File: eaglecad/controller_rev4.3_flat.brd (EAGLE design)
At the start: 40 x 29.5 mm, 79 parts, among them U100 STM32L452XX_QFPN48, U101 TCAN330, U200 TPS63070, U300 STSPIN230, U301 TSV991ILT, U302 AS5047P, U400 STSPIN250, U401 TSV991ILT, X101 ABM10-16MHz

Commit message: board flattening
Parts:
- added TP1, TP10, TP11, TP12, TP13, TP14, TP15, TP16, TP17, TP18, TP19, TP2, TP20, TP21, TP22, TP23, TP24, TP25, TP26, TP27, TP28, TP29, TP3, TP30, TP31, TP4, TP5, TP6, TP7, TP8, TP9: TEST-POINT-LARGE, oresat-misc:1X01
- moved C204 79.1 mm to (-11.7, 58.7), flipped to the bottom, turned to 180 degrees
- moved R203 79.1 mm to (-13.6, 58.7), flipped to the bottom, turned to 0 degrees
- moved R205 78.9 mm to (-10.2, 58.5), flipped to the bottom, turned to 270 degrees
- moved C207 78.4 mm to (-8.71, 58.1), flipped to the bottom, turned to 90 degrees
- moved R202 78.4 mm to (-15.5, 58.1), flipped to the bottom, turned to 180 degrees
- moved C202 78.1 mm to (-17.8, 57.9), flipped to the bottom, turned to 90 degrees
- moved R201 77.1 mm to (-15.2, 57.1), flipped to the bottom, turned to 0 degrees
- moved U200 76.6 mm to (-12.5, 56.7), flipped to the bottom, turned to 270 degrees
- moved R204 76.6 mm to (-10.2, 56.6), flipped to the bottom, turned to 270 degrees
- moved C401 75.0 mm to (51.1, 76.3), flipped to the bottom, turned to 90 degrees
- moved C402 75.0 mm to (49.6, 76.3), flipped to the bottom, turned to 90 degrees
- moved C403 75.0 mm to (48.1, 76.3), flipped to the bottom, turned to 90 degrees
- moved C203 74.7 mm to (-15.9, 55.1), flipped to the bottom, turned to 270 degrees
- moved C205 74.5 mm to (-8.96, 54.9), flipped to the bottom, turned to 270 degrees
- moved C206 74.2 mm to (-7.21, 54.6), flipped to the bottom, turned to 270 degrees
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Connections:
- net 3.3V: now also TP29.1, TP30.1, TP31.1
- net ADDR_0: now also TP14.1
- net ADDR_1: now also TP15.1
- net BLDC_CURR_FDB: now also TP2.1
- net BLDC_EN: now also TP11.1
- net BLDC_FAULT: now also TP10.1
- net BLDC_INUH: now also TP23.1
- net BLDC_INUL: now also TP7.1
- net BLDC_INVH: now also TP24.1
- net BLDC_INVL: now also TP8.1
- net BLDC_INWH: now also TP25.1
- net BLDC_INWL: now also TP9.1
- net BLDC_STBY: now also TP22.1
- net CAN_RX: now also TP27.1
- net CAN_SILENT: now also TP28.1
- net CAN_TX: now also TP26.1
- net DEBUG_1: now also TP13.1
- net DEBUG_2: now also TP6.1
- net I2C_SCL: now also TP20.1
- net I2C_SDA: now also TP21.1
- net MAG_CURR_FDB: now also TP1.1
- net MAG_DIR: now also TP16.1
- net MAG_EN: now also TP19.1
- net MAG_FAULT: now also TP18.1
- net MAG_PWM: now also TP12.1
- net MAG_STBY: now also TP17.1
- net SPI1_CS: now also TP3.1
- net SPI1_MISO: now also TP5.1
- net SPI1_SCK: now also TP4.1
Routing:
- net GND: track 59.1 -> 0.00 mm, vias 179 -> 0
- net 3.3V: track 29.8 -> 0.00 mm, vias 18 -> 0
- net I2C_SCL: track 26.9 -> 0.00 mm, vias 2 -> 0
- net BLDC_CURR_FDB: track 25.8 -> 0.00 mm, vias 2 -> 0
- net I2C_SDA: track 25.1 -> 0.00 mm, vias 2 -> 0
- net BOOT: track 19.7 -> 0.00 mm, vias 2 -> 0
- net MAG_CURR_FDB: track 17.8 -> 0.00 mm, vias 2 -> 0
- net SWCLK: track 17.6 -> 0.00 mm, vias 2 -> 0
- net SWDIO: track 17.3 -> 0.00 mm, vias 2 -> 0
- net SENSE_BLDC: track 16.6 -> 0.00 mm, vias 3 -> 0
- net OUT1: track 15.8 -> 0.00 mm, vias 3 -> 0
- net BLDC_STBY: track 15.7 -> 0.00 mm, vias 2 -> 0
- net SPI1_CS: track 14.8 -> 0.00 mm, vias 1 -> 0
- net BLDC_INUH: track 14.5 -> 0.00 mm
- net SPI1_MISO: track 14.0 -> 0.00 mm, vias 1 -> 0
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- added copper zone on layer 16, net 3.3V
- added copper zone on layer 16, net TPS-L5
- added copper zone on layer 16, net TPS-L6
- removed copper zone on layer 1, net 3.3V
- removed copper zone on layer 15, net 3.3V
- removed copper zone on layer 1, net GND
- removed copper zone on layer 16, net GND
- removed copper zone on layer 1, net TPS-L5
- removed copper zone on layer 1, net TPS-L6
- removed copper zone on layer 1, net VBUS
- removed copper zone on layer 15, net VBUS

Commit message: Flattening the board
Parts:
- removed C501: DEBUG_CON, oresat-ACS_driver_board:DEBUG_CON
- added DEBUG1: (no value), pinhead:1X02
- added J1: (no value), SparkFun-Connectors:6_PIN_SERIAL_TARGET_SIDE_W_SILK
- added LED5, LED6: BLUE, led:CHIPLED_0603
- added LED7: AMBER, led:CHIPLED_0603
- added LED8: GREEN, led:CHIPLED_0603
- added R5, R6: 100, oresat-rcl:.0402-B-NOSILK
- added R7: 1.3k, oresat-rcl:.0402-B-NOSILK
- added R8: 330, oresat-rcl:.0402-B-NOSILK
- added SWD1: 1.27MM-SWD-CONNECTOR, J-CNC-3220-10-0100-00-ARM-SWD-port:1.27MM_2X5
- moved C401 65.0 mm to (-13.8, 72.1), turned to 0 degrees
- moved C402 63.6 mm to (-13.8, 70.6), turned to 0 degrees
- moved C403 62.3 mm to (-13.8, 69.1), turned to 0 degrees
- moved R411 56.1 mm to (-0.69, 69.0), turned to 0 degrees
- moved R412 54.5 mm to (-0.69, 67.0), turned to 0 degrees
- moved C410 51.2 mm to (3.62, 69.7), turned to 90 degrees
- moved R409 51.0 mm to (2.17, 70.2), turned to 0 degrees
- moved R405 50.8 mm to (1.96, 67.0), turned to 270 degrees
- moved R410 50.7 mm to (2.17, 69.2)
- moved R406 49.8 mm to (3.41, 67.5), turned to 180 degrees
- moved C409 49.4 mm to (6.22, 72.7)
- moved U401 49.3 mm to (5.93, 70.3), turned to 180 degrees
- moved R414 49.1 mm to (8.72, 68.3)
- moved C411 49.1 mm to (8.23, 69.8)
- moved R413 49.1 mm to (9.23, 69.8)
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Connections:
- new net N$5: LED5.C, R5.2
- new net N$6: LED6.C, R6.2
- new net N$7: LED7.C, R7.2
- new net N$8: LED8.C, R8.2
- net 3.3V: now also LED8.A, SWD1.VTREF; no longer C501.3.3V
- net DEBUG_1: now also DEBUG1.1, LED6.A; no longer C501.DEBUG_1
- net DEBUG_2: now also DEBUG1.2, LED5.A; no longer C501.DEBUG_2
- net GND: now also J1.P$6, R5.1, R6.1, R7.1, R8.1, SWD1.GND, SWD1.GND@2; no longer C501.GND
- net NRST: now also SWD1.!RESET; no longer C501.NRST
- net SWCLK: now also SWD1.SWDCLK; no longer C501.SWCLK
- net SWDIO: now also SWD1.SWDIO; no longer C501.SWDIO
- net UART_RX: now also J1.P$3; no longer C501.UART_RX
- net UART_TX: now also J1.P$2; no longer C501.UART_TX
- net VBUS: now also J1.P$4, LED7.A; no longer C501.VBUS
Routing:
- net GND: track 0.00 -> 31.6 mm, vias 0 -> 4
- net 3.3V: track 0.00 -> 24.4 mm, vias 0 -> 3
- net CAN_SILENT: track 0.00 -> 16.0 mm
- net BLDC_STBY: track 0.00 -> 14.7 mm, vias 0 -> 2
- net BLDC_INWL: track 0.00 -> 13.3 mm, vias 0 -> 1
- net BLDC_FAULT: track 0.00 -> 13.2 mm
- net BLDC_INUH: track 0.00 -> 12.7 mm
- net MAG_FAULT: track 0.00 -> 12.7 mm
- net MAG_STBY: track 0.00 -> 12.7 mm
- net SENSE_BLDC: track 0.00 -> 12.5 mm, vias 0 -> 2
- net CAN_RX: track 0.00 -> 12.1 mm
- net BLDC_INUL: track 0.00 -> 12.1 mm
- net BLDC_INWH: track 0.00 -> 12.0 mm, vias 0 -> 1
- net BLDC_INVL: track 0.00 -> 11.6 mm
- net CAN_TX: track 0.00 -> 11.2 mm
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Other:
- board text added: "3.3V"
- board text added: "ACS DRIVER PROG ADAPTER"
- board text added: "DBUG1"
- board text added: "DBUG2"
- board text added: "Eric Ruhl"
- board text added: "GND"
- board text added: "NRST"
- board text added: "RX"
- board text added: "SWCLK"
- board text added: "SWDIO"
- board text added: "TX"
- board text added: "VBUS"
- board text added: "rev 1.1"
- board text removed: "ACS Driver OreSat Rev 4.2B Eric Ruhl"

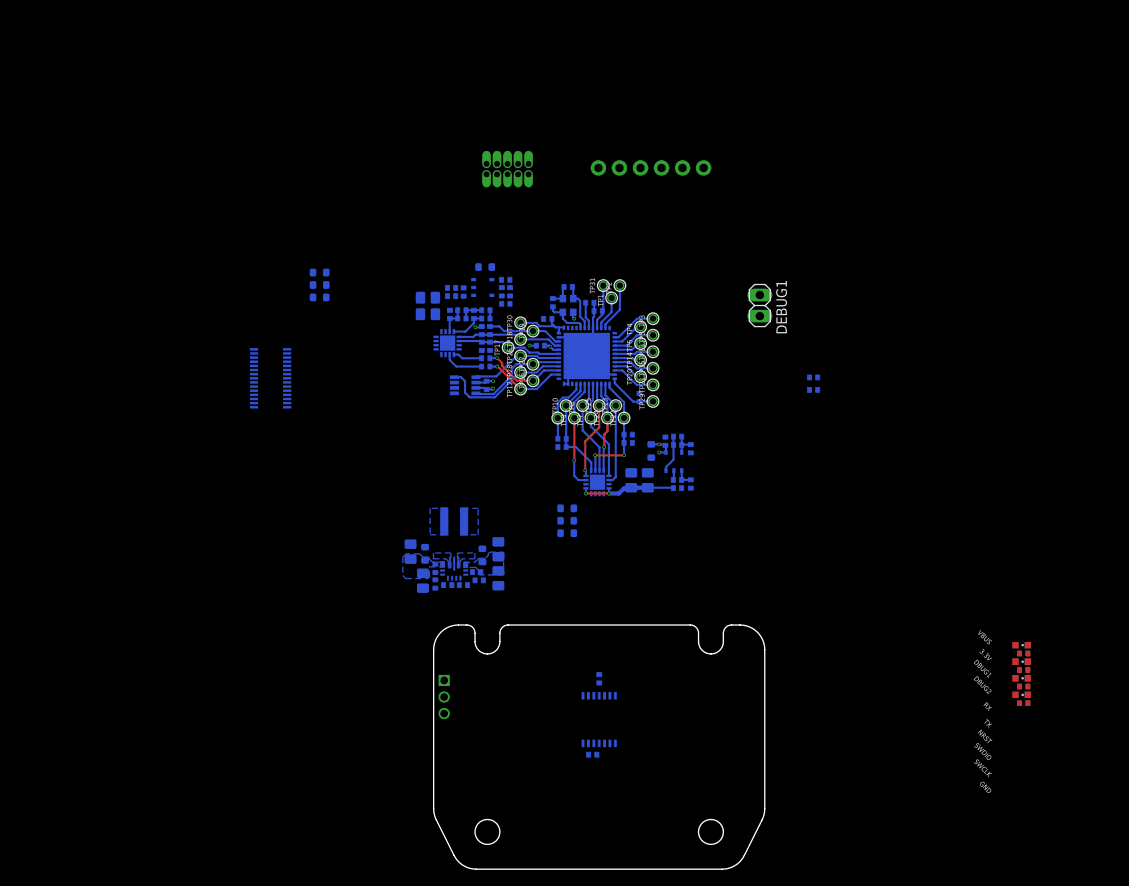
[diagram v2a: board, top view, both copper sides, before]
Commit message: Flattening rev 4.3
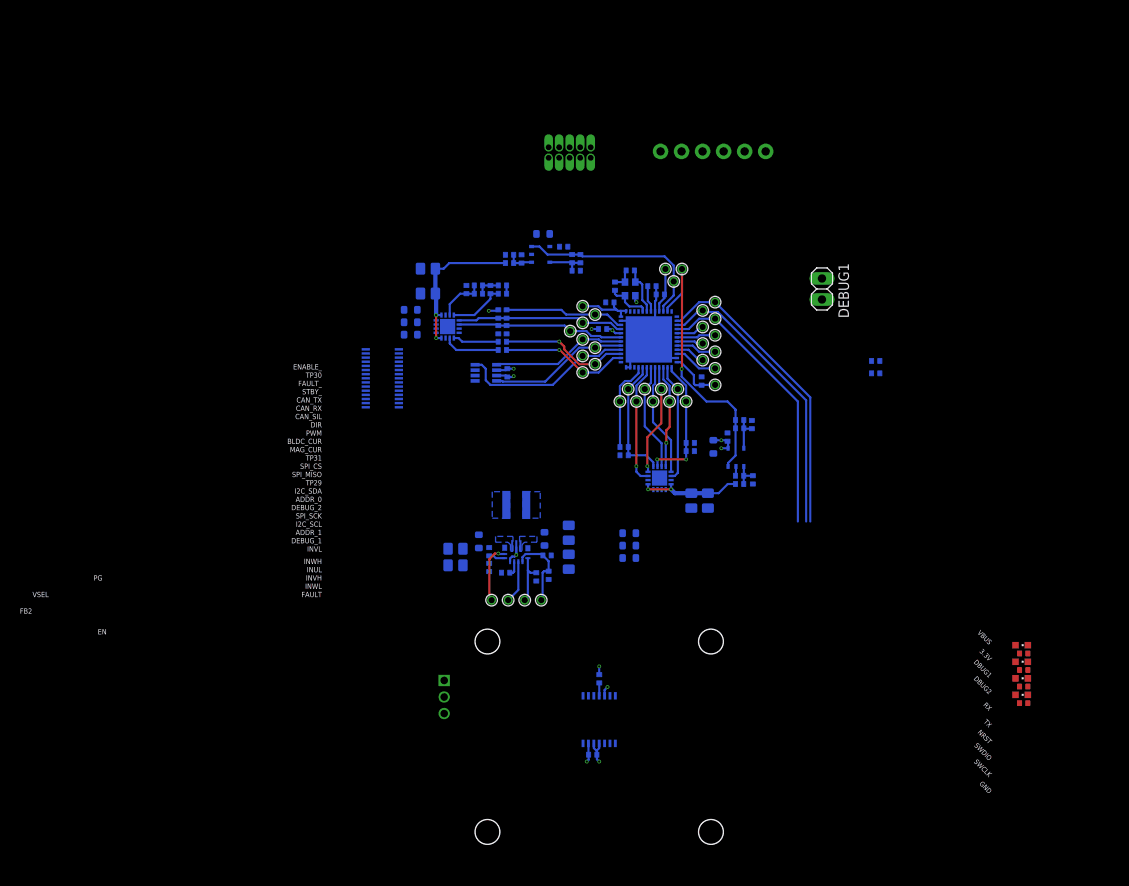
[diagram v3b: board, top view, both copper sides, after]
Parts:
- removed TP1, TP10, TP11, TP12, TP13, TP14, TP15, TP16, TP17, TP18, TP19, TP2, TP20, TP21, TP22, TP23, TP24, TP25, TP26, TP27, TP28, TP3, TP4, TP5, TP6, TP7, TP8, TP9: TEST-POINT-LARGE, oresat-misc:1X01
- added ADDR_0, ADDR_1, BLDC_CUR, CAN_RX, CAN_SIL, CAN_TX, DEBUG_1, DEBUG_2, DIR, EN, ENABLE, ENABLE_, FAULT, FAULT_, FB2, I2C_SCL, I2C_SDA, INUH, INUL, INVH, INVL, INWH, INWL, MAG_CUR, PG, PWM, SPI_CS, SPI_MISO, SPI_SCK, STBY, STBY_, VSEL: TEST-POINT-LARGE, oresat-misc:1X01
- moved U$2 13.5 mm to (-6.20, 59.3)
- moved C401 11.9 mm to (-2.77, 67.6)
- moved C402 11.9 mm to (-2.77, 66.1)
- moved C403 11.9 mm to (-2.77, 64.6)
- moved C411 9.39 mm to (16.7, 73.8)
- moved R413 9.39 mm to (17.7, 73.8)
- moved R414 9.39 mm to (17.2, 72.3)
- moved R203 8.86 mm to (12.4, 35.3), turned to 90 degrees
- moved C201 8.73 mm to (16.3, 40.6)
- moved C202 8.73 mm to (16.3, 37.1)
- moved R201 8.73 mm to (13.7, 37.9)
- moved R202 8.41 mm to (13.9, 35.5), turned to 90 degrees
- moved C301 8.08 mm to (23.6, 40.6)
- moved C302 8.08 mm to (23.6, 39.1)
- moved C303 8.08 mm to (23.6, 37.6)
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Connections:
- new net FB2: FB2.1, U200.6
- new net PG: PG.1, U200.2
- net ADDR_0: now also ADDR_0.1; no longer TP14.1
- net ADDR_1: now also ADDR_1.1; no longer TP15.1
- net BLDC_CURR_FDB: now also BLDC_CUR.1; no longer TP2.1
- net BLDC_EN: now also ENABLE.1; no longer TP11.1
- net BLDC_FAULT: now also FAULT.1; no longer TP10.1
- net BLDC_INUH: now also INUH.1; no longer TP23.1
- net BLDC_INUL: now also INUL.1; no longer TP7.1
- net BLDC_INVH: now also INVH.1; no longer TP24.1
- net BLDC_INVL: now also INVL.1; no longer TP8.1
- net BLDC_INWH: now also INWH.1; no longer TP25.1
- net BLDC_INWL: now also INWL.1; no longer TP9.1
- net BLDC_STBY: now also STBY.1; no longer TP22.1
- net CAN_RX: now also CAN_RX.1; no longer TP27.1
- net CAN_SILENT: now also CAN_SIL.1; no longer TP28.1
- net CAN_TX: now also CAN_TX.1; no longer TP26.1
- net DEBUG_1: now also DEBUG_1.1; no longer TP13.1
- net DEBUG_2: now also DEBUG_2.1; no longer TP6.1
- net I2C_SCL: now also I2C_SCL.1; no longer TP20.1
- net I2C_SDA: now also I2C_SDA.1; no longer TP21.1
- net MAG_CURR_FDB: now also MAG_CUR.1; no longer TP1.1
- net MAG_DIR: now also DIR.1; no longer TP16.1
- net MAG_EN: now also ENABLE_.1; no longer TP19.1
- net MAG_FAULT: now also FAULT_.1; no longer TP18.1
- net MAG_PWM: now also PWM.1; no longer TP12.1
- net MAG_STBY: now also STBY_.1; no longer TP17.1
- net SPI1_CS: now also SPI_CS.1; no longer TP3.1
- net SPI1_MISO: now also SPI_MISO.1; no longer TP5.1
- net SPI1_SCK: now also SPI_SCK.1; no longer TP4.1
- net TPS-EN2: now also EN.1
- net TPS-VSEL2: now also VSEL.1
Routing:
- net SPI1_SCK: track 3.85 -> 35.5 mm
- net SPI1_CS: track 5.56 -> 36.8 mm
- net SPI1_MISO: track 5.14 -> 33.8 mm
- net BLDC_CURR_FDB: track 10.3 -> 34.3 mm, vias 0 -> 1
- net MAG_CURR_FDB: track 4.14 -> 24.2 mm
- net SENSE_MAG: track 0.00 -> 18.4 mm, vias 0 -> 2
- net TPS-EN2: track 0.00 -> 9.62 mm
- net MAG_FAULT: track 12.7 -> 20.2 mm
- net MAG_STBY: track 12.7 -> 20.2 mm
- net FB2: track 0.00 -> 7.21 mm, vias 0 -> 1
- net TPS-VSEL2: track 0.00 -> 6.38 mm
- net GND: track 31.6 -> 37.7 mm, vias 4 -> 7
- net MAG_PWM: track 10.2 -> 15.7 mm
- net MAG_EN: track 9.07 -> 14.6 mm
- net MAG_DIR: track 10.2 -> 15.7 mm
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- removed copper zone on layer 16, net 3.3V
- removed copper zone on layer 16, net VBUS
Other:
- board outline removed
- board text added: "ACS Driver OreSat Rev 4.3_flat Eric Ruhl"
- board text removed: "ACS Driver OreSat Rev 4.3 Eric Ruhl"

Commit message: traces routed, still needs polygons and planes
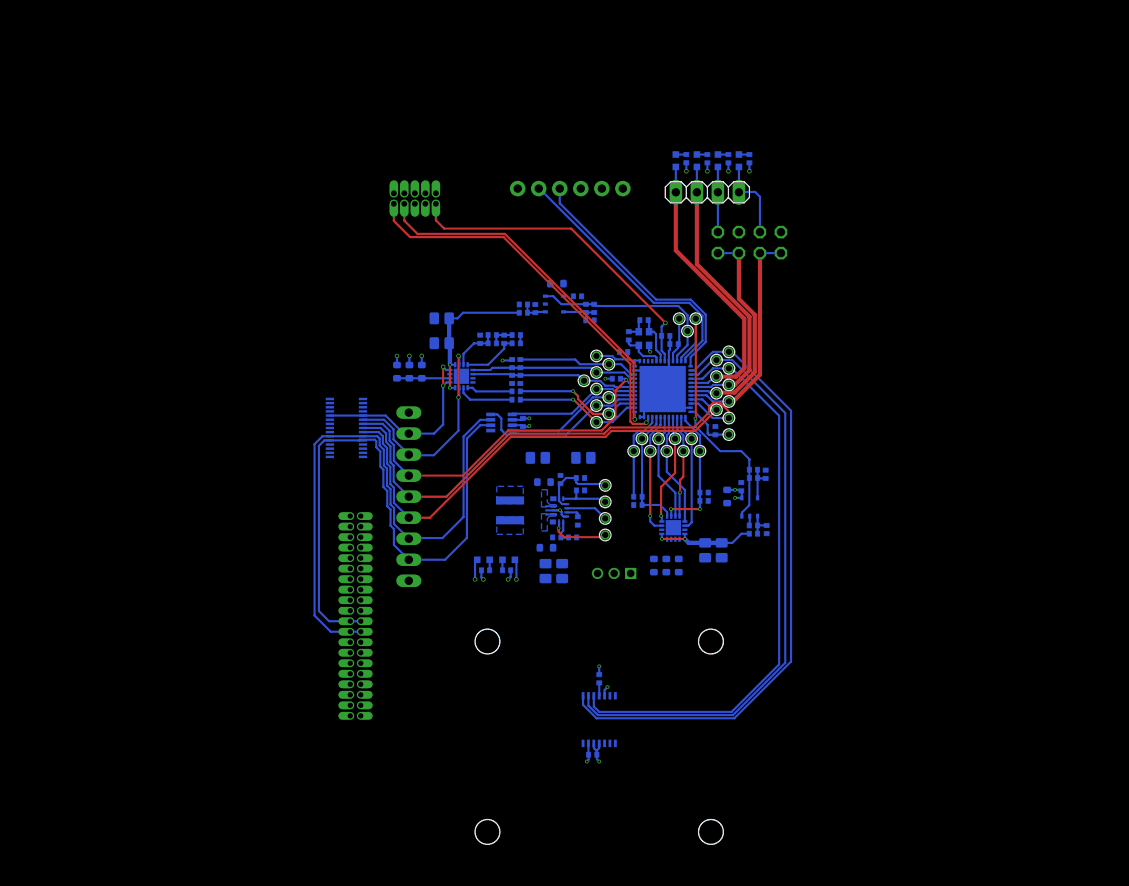
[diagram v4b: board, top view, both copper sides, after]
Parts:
- removed DEBUG1: (no value), pinhead:1X02
- removed R102, R103: 0, rcl_custom:.0402-B-NOSILK
- removed R7: 1.3k, oresat-rcl:.0402-B-NOSILK
- removed R8: 330, oresat-rcl:.0402-B-NOSILK
- added J2: J-SAMTEC-TFM-120-X1-XXX-D-RA, J-Samtec-TFM-120-X1-XXX-D-RA:J-SAMTEC-TFM-120-X1-XXX-D-RA
- added JP1: (no value), pinhead:1X04
- added JP2: (no value), pinhead:2X04
- added JP3: (no value), pinhead:1X09
- added LED1, LED2: BLUE, led:CHIPLED_0603
- added R1: 1.3k, oresat-rcl:.0402-B-NOSILK
- added R2: 330, oresat-rcl:.0402-B-NOSILK
- added R3, R4: 100, oresat-rcl:.0402-B-NOSILK
- moved LED5 75.5 mm to (31.8, 85.6), flipped to the bottom, turned to 0 degrees
- moved LED6 75.2 mm to (29.3, 85.6), flipped to the bottom, turned to 0 degrees
- moved R5 74.8 mm to (35.6, 85.8), flipped to the bottom, turned to 90 degrees
- moved R6 71.9 mm to (38.1, 85.8), flipped to the bottom, turned to 90 degrees
- moved LED7 65.8 mm to (6.02, 37.4), flipped to the bottom, turned to 90 degrees
- moved LED8 63.2 mm to (9.06, 37.4), flipped to the bottom
- moved JP301 25.4 mm to (21.8, 35.7), turned to 0 degrees
- moved SWD1 19.5 mm to (-2.27, 81.0)
- moved J1 17.8 mm to (16.5, 82.2)
- moved EN 15.9 mm to (20.7, 46.4), turned to 90 degrees
- moved FB2 15.8 mm to (20.7, 40.4), turned to 90 degrees
- moved VSEL 15.3 mm to (20.7, 44.4), turned to 90 degrees
- moved PG 15.3 mm to (20.7, 42.4), turned to 90 degrees
- moved C207 12.9 mm to (15.5, 36.0), turned to 270 degrees
- moved C202 12.7 mm to (18.1, 49.7), turned to 180 degrees
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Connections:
- new net DEBUG_3: JP1.3, JP2.1, LED1.A
- new net DEBUG_4: JP1.4, JP2.5, LED2.A
- new net N$1: LED1.C, R5.2
- new net N$2: LED2.C, R6.2
- new net V_BATT: J2.21, J2.22, J2.23, J2.24, J2.25, J2.26
- net ADDR_0: now also JP2.2, JP2.4; no longer R102.2
- net ADDR_1: now also JP2.6, JP2.8; no longer R103.2
- net BOOT: now also JP3.6
- net CAN_H: now also J2.17, J2.18, JP3.3
- net CAN_L: now also J2.19, J2.20, JP3.2
- net DEBUG_1: now also JP1.1, U100.17; no longer DEBUG1.1, U100.18
- net DEBUG_2: now also JP1.2, U100.18; no longer DEBUG1.2, U100.17
- net GND: now also J2.27, J2.28, J2.29, J2.30, J2.31, J2.32, J2.37, J2.38, JP2.3, JP2.7, JP3.9, R1.1, R2.1, R3.1, R4.1; no longer R102.1, R103.1, R7.1, R8.1
- net I2C_SCL: now also JP3.4
- net I2C_SDA: now also JP3.5
- net N$5: now also R4.2; no longer R5.2
- net N$6: now also R3.2; no longer R6.2
- net N$7: now also R1.2; no longer R7.2
- net N$8: now also R2.2; no longer R8.2
- net OUT1: now also JP3.7
- net OUT2: now also JP3.8
- net VBUS: now also JP3.1
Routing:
- net CAN_L: track 0.00 -> 72.9 mm
- net CAN_H: track 0.00 -> 70.6 mm
- net I2C_SDA: track 5.35 -> 62.2 mm
- net I2C_SCL: track 3.64 -> 60.0 mm
- net SWDIO: track 0.00 -> 47.6 mm, vias 0 -> 1
- net SWCLK: track 0.00 -> 44.7 mm, vias 0 -> 1
- net BOOT: track 1.92 -> 44.8 mm
- net SPI1_CS: track 36.8 -> 76.0 mm
- net SPI1_SCK: track 35.5 -> 73.1 mm
- net NRST: track 3.21 -> 39.8 mm, vias 0 -> 1
- net SPI1_MISO: track 33.8 -> 70.0 mm
- net UART_TX: track 0.00 -> 32.5 mm
- net UART_RX: track 0.00 -> 32.0 mm
- net DEBUG_2: track 3.44 -> 35.1 mm
- net DEBUG_1: track 4.73 -> 35.0 mm
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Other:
- board text added: "ADDR_0"
- board text added: "ADDR_1"
- board text added: "DEBUG_1"
- board text added: "DEBUG_2"
- board text added: "DEBUG_3"
- board text added: "DEBUG_4"
- board text removed: "3.3V"
- board text removed: "ACS DRIVER PROG ADAPTER"
- board text removed: "DBUG1"
- board text removed: "DBUG2"
- board text removed: "Eric Ruhl"
- board text removed: "GND"
- board text removed: "NRST"
- board text removed: "RX"
- board text removed: "SWCLK"
- board text removed: "SWDIO"
- board text removed: "TX"
- board text removed: "VBUS"
- board text removed: "rev 1.1"
